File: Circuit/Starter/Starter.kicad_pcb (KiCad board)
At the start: 2 copper layers, 246.4 x 86.4 mm, 18 parts, among them J1 From Power, J2 Output+, J3 Output-, T1 BSH12-N406L 8:6400, T2 20:20, T3 20:20

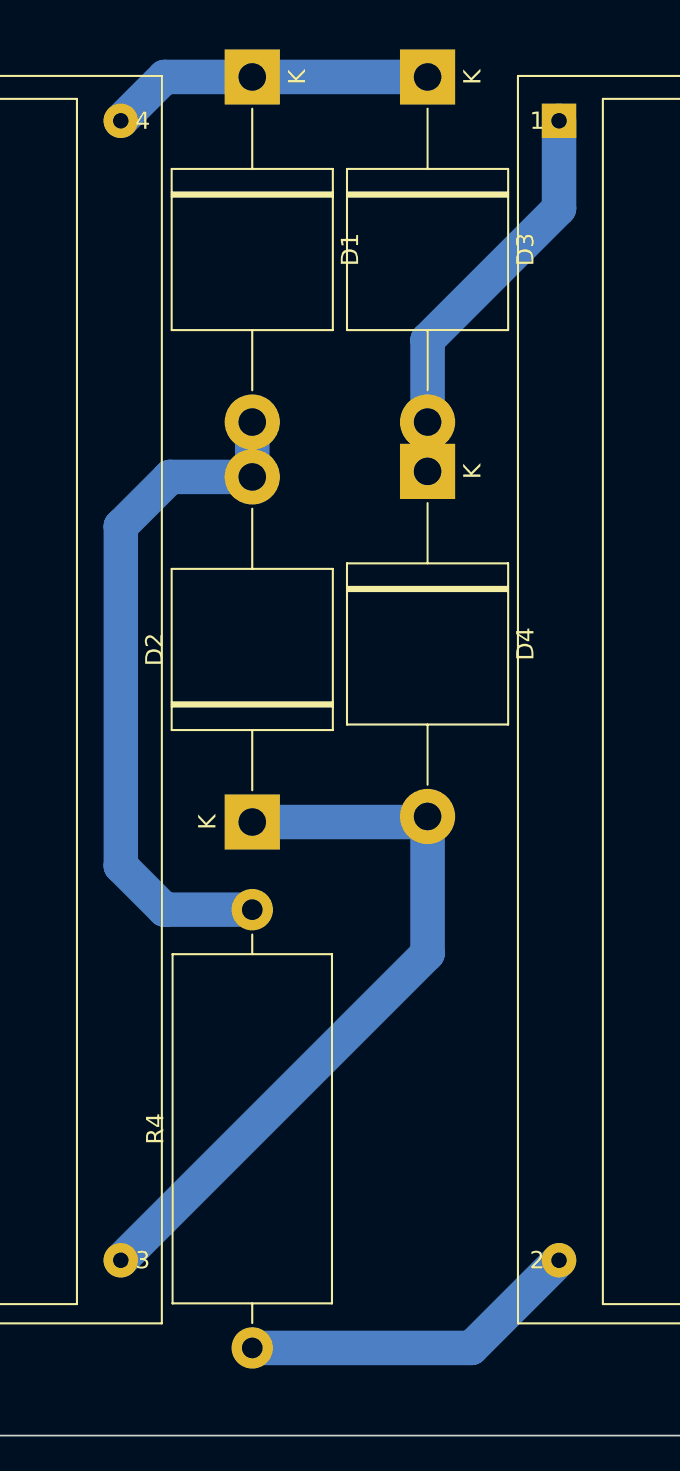
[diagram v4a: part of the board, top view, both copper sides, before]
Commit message: [Circuit] Rename the flyback transformer file
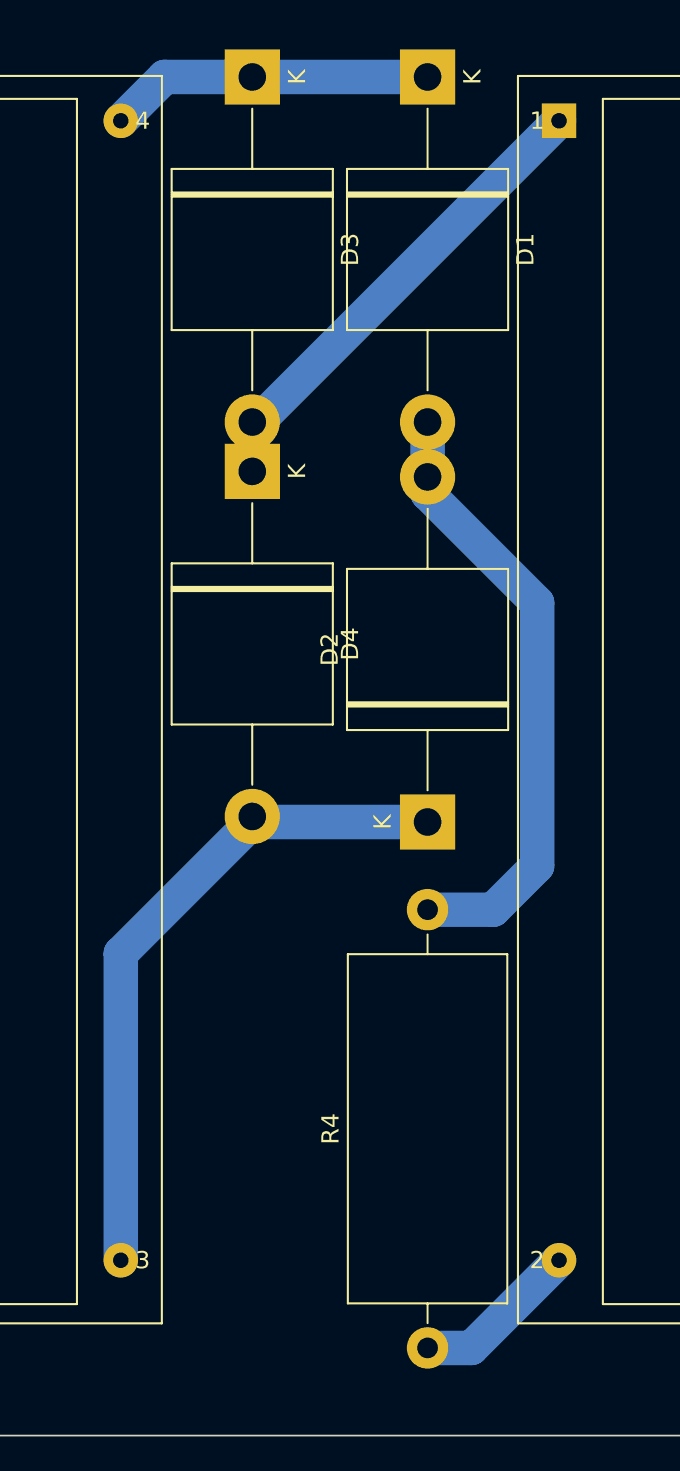
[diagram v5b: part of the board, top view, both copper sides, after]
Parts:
- moved D1 10.2 mm to (218.4, 50.8)
- moved D2 10.2 mm to (218.4, 94.0)
- moved D3 10.2 mm to (208.3, 50.8)
- moved D4 10.2 mm to (208.3, 73.7)
- moved R4 10.2 mm to (218.4, 124.5)
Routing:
- net Net-(R4-Pad1): track 19.9 -> 9.72 mm
- net Net-(D1-Pad2): track 41.0 -> 35.8 mm
- net Net-(D2-Pad1): track 43.4 -> 38.8 mm
- net Net-(D3-Pad2): track 23.8 -> 27.6 mm
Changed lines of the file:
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@@
     (thickness 1.6)
     (drawings 4)
-    (tracks 48)
+    (tracks 43)
     (zones 0)
     (modules 18)
@@
   )
   (module Diode_THT:D_P600_R-6_P20.00mm_Horizontal (layer F.Cu)
-    (at 218.44 73.66 270)
+    (at 208.28 73.66 270)
     (descr "Diode, P600_R-6 series, Axial, Horizontal, pin pitch=20mm, , length*diameter=9.1*9.1mm^2, , http://www.vishay.com/docs/88692/p600a.pdf, http://www.diodes.com/_files/packages/R-6.pdf")
     (tags "Diode P600_R-6 series Axial Horizontal pin pitch 20mm  length 9.1mm diameter 9.1mm")
@@
   )
   (module Diode_THT:D_P600_R-6_P20.00mm_Horizontal (layer F.Cu)
-    (at 218.44 50.8 270)
+    (at 208.28 50.8 270)
     (descr "Diode, P600_R-6 series, Axial, Horizontal, pin pitch=20mm, , length*diameter=9.1*9.1mm^2, , http://www.vishay.com/docs/88692/p600a.pdf, http://www.diodes.com/_files/packages/R-6.pdf")
     (tags "Diode P600_R-6 series Axial Horizontal pin pitch 20mm  length 9.1mm diameter 9.1mm")
@@
   )
   (module Diode_THT:D_P600_R-6_P20.00mm_Horizontal (layer F.Cu)
-    (at 208.28 93.98 90)
+    (at 218.44 93.98 90)
     (descr "Diode, P600_R-6 series, Axial, Horizontal, pin pitch=20mm, , length*diameter=9.1*9.1mm^2, , http://www.vishay.com/docs/88692/p600a.pdf, http://www.diodes.com/_files/packages/R-6.pdf")
     (tags "Diode P600_R-6 series Axial Horizontal pin pitch 20mm  length 9.1mm diameter 9.1mm")
@@
   )
   (module Diode_THT:D_P600_R-6_P20.00mm_Horizontal (layer F.Cu)
-    (at 208.28 50.8 270)
+    (at 218.44 50.8 270)
     (descr "Diode, P600_R-6 series, Axial, Horizontal, pin pitch=20mm, , length*diameter=9.1*9.1mm^2, , http://www.vishay.com/docs/88692/p600a.pdf, http://www.diodes.com/_files/packages/R-6.pdf")
     (tags "Diode P600_R-6 series Axial Horizontal pin pitch 20mm  length 9.1mm diameter 9.1mm")
@@
   )
   (module Resistor_THT:R_Axial_DIN0922_L20.0mm_D9.0mm_P25.40mm_Horizontal (layer F.Cu)
-    (at 208.28 124.46 90)
+    (at 218.44 124.46 90)
     (descr "Resistor, Axial_DIN0922 series, Axial, Horizontal, pin pitch=25.4mm, 5W, length*diameter=20*9mm^2, http://www.vishay.com/docs/20128/wkxwrx.pdf")
     (tags "Resistor Axial_DIN0922 series Axial Horizontal pin pitch 25.4mm 5W length 20mm diameter 9mm")
@@
   (segment (start 172.72 119.38) (end 165.1 127) (width 2) (layer B.Cu) (net 3) (status 10))
   (segment (start 165.1 127) (end 76.2 127) (width 2) (layer B.Cu) (net 3))
-  (segment (start 208.28 73.98) (end 208.28 70.8) (width 2) (layer B.Cu) (net 4) (status 30))
-  (segment (start 208.6 73.98) (end 208.28 73.98) (width 2) (layer B.Cu) (net 4) (status 30))
-  (segment (start 208.28 73.98) (end 207.96 73.98) (width 2) (layer B.Cu) (net 4) (status 30))
-  (segment (start 208.28 73.98) (end 203.52 73.98) (width 2) (layer B.Cu) (net 4) (status 10))
-  (segment (start 203.52 73.98) (end 200.66 76.84) (width 2) (layer B.Cu) (net 4))
-  (segment (start 200.66 76.84) (end 200.66 96.52) (width 2) (layer B.Cu) (net 4))
-  (segment (start 203.2 99.06) (end 208.28 99.06) (width 2) (layer B.Cu) (net 4) (status 20))
-  (segment (start 200.66 96.52) (end 203.2 99.06) (width 2) (layer B.Cu) (net 4))
+  (segment (start 218.44 70.8) (end 218.44 73.98) (width 2) (layer B.Cu) (net 4))
+  (segment (start 222.25 99.06) (end 218.44 99.06) (width 2) (layer B.Cu) (net 4))
+  (segment (start 224.79 96.52) (end 222.25 99.06) (width 2) (layer B.Cu) (net 4))
+  (segment (start 218.44 74.93) (end 224.79 81.28) (width 2) (layer B.Cu) (net 4))
+  (segment (start 218.44 73.98) (end 218.44 74.93) (width 2) (layer B.Cu) (net 4))
+  (segment (start 224.79 81.28) (end 224.79 96.52) (width 2) (layer B.Cu) (net 4))
   (segment (start 208.28 50.8) (end 218.44 50.8) (width 2) (layer B.Cu) (net 5) (status 30))
   (segment (start 203.2 50.8) (end 200.66 53.34) (width 2) (layer B.Cu) (net 5) (status 20))
@@
   (segment (start 254 53.34) (end 264.16 53.34) (width 2) (layer B.Cu) (net 9) (status 30))
   (segment (start 254 119.38) (end 264.16 119.38) (width 2) (layer B.Cu) (net 10) (status 30))
-  (segment (start 226.06 119.38) (end 220.98 124.46) (width 2) (layer B.Cu) (net 11) (status 10))
-  (segment (start 208.28 124.46) (end 220.98 124.46) (width 2) (layer B.Cu) (net 11) (status 10))
+  (segment (start 220.98 124.46) (end 226.06 119.38) (width 2) (layer B.Cu) (net 11))
+  (segment (start 218.44 124.46) (end 220.98 124.46) (width 2) (layer B.Cu) (net 11))
   (segment (start 55.88 66.04) (end 55.88 60.96) (width 2) (layer B.Cu) (net 12) (status 30))
   (segment (start 55.88 96.52) (end 55.88 111.76) (width 2) (layer B.Cu) (net 13) (status 20))
   (segment (start 38.1 68.58) (end 38.1 78.74) (width 2) (layer B.Cu) (net 13) (status 10))
   (segment (start 38.1 78.74) (end 55.88 96.52) (width 2) (layer B.Cu) (net 13))
-  (segment (start 218.12 93.98) (end 218.44 93.66) (width 2) (layer B.Cu) (net 14) (status 30))
-  (segment (start 208.28 93.98) (end 218.12 93.98) (width 2) (layer B.Cu) (net 14) (status 30))
-  (segment (start 200.66 119.38) (end 218.44 101.6) (width 2) (layer B.Cu) (net 14) (status 10))
-  (segment (start 218.44 101.6) (end 218.44 93.66) (width 2) (layer B.Cu) (net 14) (status 20))
-  (segment (start 218.44 70.8) (end 218.44 73.66) (width 2) (layer B.Cu) (net 15) (status 30))
-  (segment (start 218.44 70.8) (end 218.76 70.8) (width 2) (layer B.Cu) (net 15) (status 30))
-  (segment (start 226.06 53.34) (end 226.06 58.42) (width 2) (layer B.Cu) (net 15) (status 10))
-  (segment (start 218.44 66.04) (end 226.06 58.42) (width 2) (layer B.Cu) (net 15))
-  (segment (start 218.44 70.8) (end 218.44 66.04) (width 2) (layer B.Cu) (net 15) (status 10))
+  (segment (start 200.66 101.6) (end 208.28 93.98) (width 2) (layer B.Cu) (net 14))
+  (segment (start 200.66 119.38) (end 200.66 101.6) (width 2) (layer B.Cu) (net 14))
+  (segment (start 218.12 93.98) (end 218.44 93.66) (width 2) (layer B.Cu) (net 14))
+  (segment (start 208.28 93.98) (end 218.12 93.98) (width 2) (layer B.Cu) (net 14))
+  (segment (start 208.6 70.8) (end 226.06 53.34) (width 2) (layer B.Cu) (net 15))
+  (segment (start 208.28 70.8) (end 208.28 73.66) (width 2) (layer B.Cu) (net 15))
 )

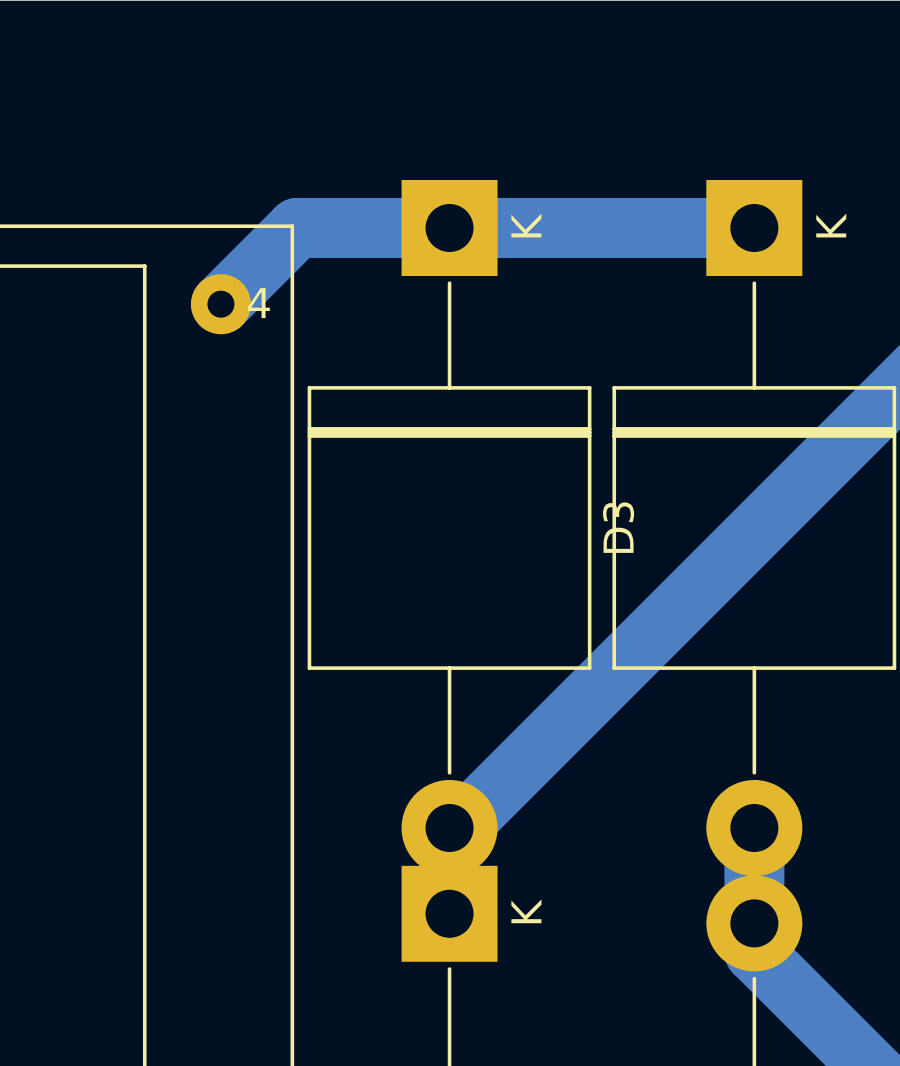
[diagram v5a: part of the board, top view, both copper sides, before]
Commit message: [Circuit] Fix the direction of diode in starter
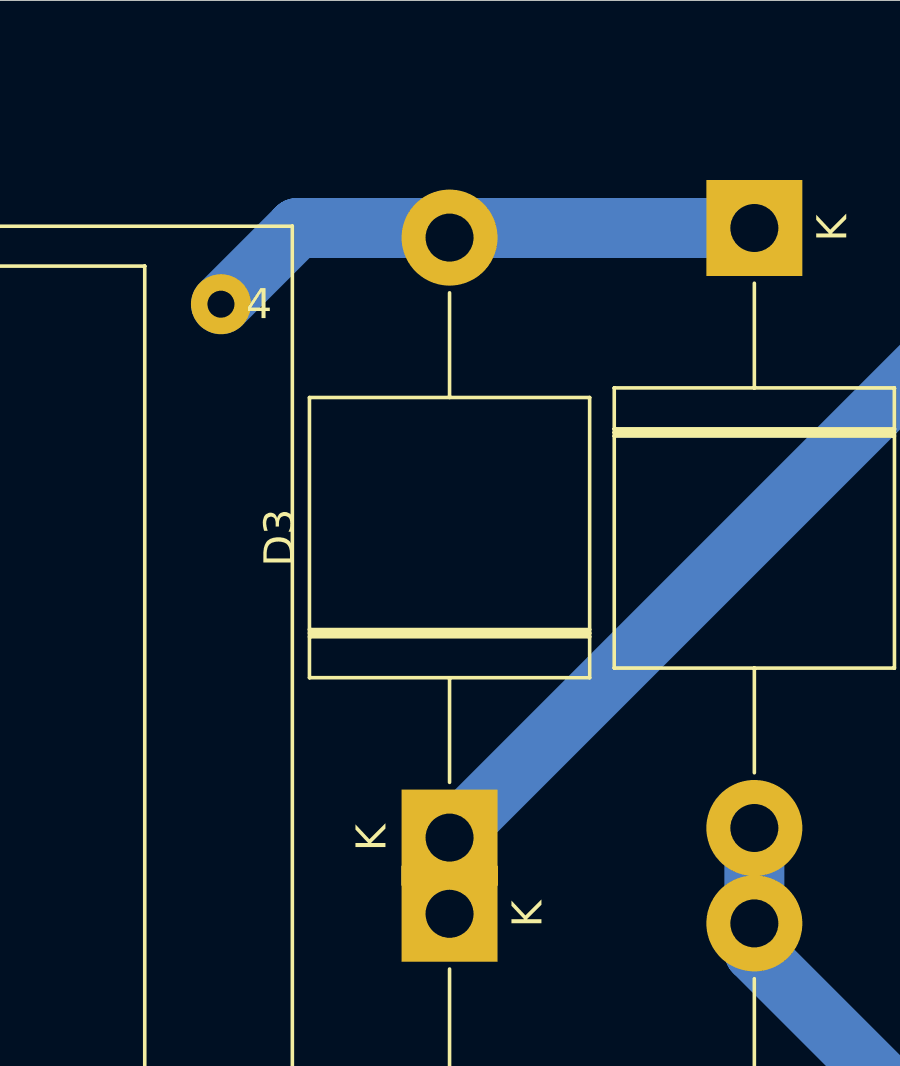
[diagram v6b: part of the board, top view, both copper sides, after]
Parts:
- T1: footprint Power:FlybackTransformer_BSH12-N406L -> Power:Flyback_Transformer_BSH12-N406L
- moved D3 20.3 mm to (208.3, 71.1), turned to 90 degrees
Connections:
- D3 pad 1: Net-(D1-Pad1) -> Net-(D3-Pad1)
- D3 pad 2: Net-(D3-Pad2) -> Net-(D1-Pad1)
- D4 pad 1: Net-(D3-Pad2) -> Net-(D3-Pad1)
- T3 pad 1: Net-(D3-Pad2) -> Net-(D3-Pad1)
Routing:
- net Net-(D3-Pad2): track 27.6 -> 0.00 mm
- net Net-(D3-Pad1): track 0.00 -> 27.6 mm
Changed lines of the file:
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@@
   (net 13 "Net-(L2-Pad1)")
   (net 14 "Net-(D2-Pad1)")
-  (net 15 "Net-(D3-Pad2)")
+  (net 15 "Net-(D3-Pad1)")
   (net_class Default "This is the default net class."
     (clearance 0.2)
@@
     (add_net "Net-(D1-Pad2)")
     (add_net "Net-(D2-Pad1)")
-    (add_net "Net-(D3-Pad2)")
+    (add_net "Net-(D3-Pad1)")
     (add_net "Net-(E1-Pad2)")
     (add_net "Net-(L1-Pad1)")
@@
     (add_net "Net-(R4-Pad1)")
   )
-  (module Power:FlybackTransformer_BSH12-N406L (layer F.Cu)
+  (module Power:Flyback_Transformer_BSH12-N406L (layer F.Cu)
     (at 57.15 66.04 270)
     (descr "Flyback Transformer BSH12-N406L")
@@
     (fp_line (start 30.32 69.696) (end -2.382 69.696) (layer F.SilkS) (width 0.12))
     (pad 1 thru_hole rect (at 0 0) (size 2 2) (drill 0.9) (layers *.Cu *.Mask)
-      (net 15 "Net-(D3-Pad2)"))
+      (net 15 "Net-(D3-Pad1)"))
     (pad 2 thru_hole circle (at 0 66.04) (size 2 2) (drill 0.9) (layers *.Cu *.Mask)
       (net 11 "Net-(R4-Pad1)"))
@@
       (net 14 "Net-(D2-Pad1)"))
     (pad 1 thru_hole rect (at 0 0 270) (size 3.2 3.2) (drill 1.6) (layers *.Cu *.Mask)
-      (net 15 "Net-(D3-Pad2)"))
+      (net 15 "Net-(D3-Pad1)"))
     (model ${KISYS3DMOD}/Diode_THT.3dshapes/D_P600_R-6_P20.00mm_Horizontal.wrl
       (at (xyz 0 0 0))
@@
   )
   (module Diode_THT:D_P600_R-6_P20.00mm_Horizontal (layer F.Cu)
-    (at 208.28 50.8 270)
+    (at 208.28 71.12 90)
     (descr "Diode, P600_R-6 series, Axial, Horizontal, pin pitch=20mm, , length*diameter=9.1*9.1mm^2, , http://www.vishay.com/docs/88692/p600a.pdf, http://www.diodes.com/_files/packages/R-6.pdf")
     (tags "Diode P600_R-6 series Axial Horizontal pin pitch 20mm  length 9.1mm diameter 9.1mm")
@@
     (fp_line (start 5.45 4.55) (end 14.55 4.55) (layer F.Fab) (width 0.1))
     (fp_line (start 5.45 -4.55) (end 5.45 4.55) (layer F.Fab) (width 0.1))
-    (pad 2 thru_hole oval (at 20 0 270) (size 3.2 3.2) (drill 1.6) (layers *.Cu *.Mask)
-      (net 15 "Net-(D3-Pad2)"))
-    (pad 1 thru_hole rect (at 0 0 270) (size 3.2 3.2) (drill 1.6) (layers *.Cu *.Mask)
+    (pad 2 thru_hole oval (at 20 0 90) (size 3.2 3.2) (drill 1.6) (layers *.Cu *.Mask)
       (net 5 "Net-(D1-Pad1)"))
+    (pad 1 thru_hole rect (at 0 0 90) (size 3.2 3.2) (drill 1.6) (layers *.Cu *.Mask)
+      (net 15 "Net-(D3-Pad1)"))
     (model ${KISYS3DMOD}/Diode_THT.3dshapes/D_P600_R-6_P20.00mm_Horizontal.wrl
       (at (xyz 0 0 0))

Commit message: [Circuit] Adjust the sizes of components to reflect the real ones
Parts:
- D1, D2, D3, D4: footprint Diode_THT:D_P600_R-6_P20.00mm_Horizontal -> Power:Diode_2CL_Horizontal
- moved J3 42.6 mm to (304.8, 132.1)
- moved J2 40.7 mm to (304.8, 50.8)
- moved D4 40.2 mm to (246.4, 86.4)
- moved T3 38.2 mm to (264.2, 50.8)
- moved D3 38.1 mm to (246.4, 71.1)
- moved C2 16.3 mm to (111.8, 111.8)
- moved R2 16.3 mm to (111.8, 129.5)
- moved R4 16.1 mm to (233.7, 119.4)
- moved D2 13.0 mm to (221.0, 106.7)
- moved L2 12.7 mm to (45.7, 119.4)
- moved L1 11.4 mm to (45.7, 66.0)
- moved J1 11.4 mm to (20.3, 127.0)
- moved T1 11.4 mm to (47.0, 71.1)
- moved C1 10.2 mm to (55.9, 73.7)
- moved R1 10.2 mm to (55.9, 55.9)
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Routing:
- net Net-(R4-Pad1): track 9.72 -> 35.7 mm
- net Net-(D1-Pad1): track 18.8 -> 43.2 mm
- net Net-(D2-Pad1): track 38.8 -> 58.2 mm
- net Net-(D3-Pad1): track 27.6 -> 42.9 mm
- net Net-(C1-Pad2): track 61.0 -> 73.7 mm
- net Net-(E1-Pad2): track 74.0 -> 84.8 mm
- net Net-(C2-Pad2): track 146.1 -> 156.7 mm
- net Net-(C1-Pad1): track 121.5 -> 126.8 mm
- net Net-(D1-Pad2): track 35.8 -> 31.1 mm
- net Net-(L2-Pad1): track 50.5 -> 53.1 mm
- net /Output-: track 10.2 -> 12.7 mm
- net /Output+: track 10.2 -> 12.7 mm
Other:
- board size 246.4 x 86.4 mm -> 299.7 x 99.1 mm

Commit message: [Circuit] Adjust footprint of customized components and optimize the PCB design
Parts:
- E1: footprint Power:SparkGap -> Power:Spark_Gap
- R4: footprint Resistor_THT:R_Axial_DIN0922_L20.0mm_D9.0mm_P25.40mm_Horizontal -> Resistor_THT:R_Axial_DIN0922_L20.0mm_D9.0mm_P30.48mm_Horizontal
- moved D4 73.8 mm to (190.5, 134.6)
- moved D2 73.8 mm to (165.1, 154.9)
- moved D1 60.4 mm to (165.1, 73.7)
- moved D3 60.4 mm to (190.5, 94.0)
- moved T2 60.4 mm to (119.4, 73.7)
- moved R1 56.2 mm to (109.2, 38.1), turned to 270 degrees
- moved J2 56.1 mm to (248.9, 55.9)
- moved J3 56.1 mm to (248.9, 137.2)
- moved T3 56.1 mm to (208.3, 55.9)
- moved C1 50.3 mm to (91.4, 38.1), turned to 270 degrees
- moved L2 33.5 mm to (72.4, 139.7)
- moved E1 32.3 mm to (119.4, 38.1), turned to 0 degrees
- moved R4 30.9 mm to (203.2, 114.3), turned to 180 degrees
- moved J1 30.9 mm to (50.8, 121.9), turned to 180 degrees
- moved R2 30.6 mm to (109.2, 99.1), turned to 270 degrees
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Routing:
- net Net-(C2-Pad2): track 156.7 -> 47.1 mm
- net Net-(C1-Pad1): track 126.8 -> 47.1 mm
- net Net-(C1-Pad2): track 73.7 -> 27.9 mm
- net Net-(D3-Pad1): track 42.9 -> 86.1 mm
- net /PowerIn-: track 27.2 -> 8.89 mm
- net Net-(L2-Pad1): track 53.1 -> 70.9 mm
- net Net-(D1-Pad2): track 31.1 -> 47.0 mm
- net Net-(L1-Pad1): track 5.08 -> 20.3 mm
- net Net-(D2-Pad1): track 58.2 -> 43.2 mm
- net Net-(R4-Pad1): track 35.7 -> 25.0 mm
- net Net-(E1-Pad2): track 84.8 -> 75.7 mm
- net /PowerIn+: track 12.5 -> 8.89 mm
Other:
- board size 299.7 x 99.1 mm -> 215.9 x 132.1 mm
